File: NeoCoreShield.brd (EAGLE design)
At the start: 70.9 x 72.1 mm, 45 parts, among them J1 PXC-PTSM-04-RA-1778641, J10 MAGJACK, J2 PXC-PTSM-04-RA-1778641, J3 PXC-PTSM-04-RA-1778641, J4 PXC-PTSM-04-RA-1778641, J5 PXC-PTSM-04-RA-1778641, Q1 2.5A/30V/105mΩ, Q2 310mA/60V/1.6Ω, Q3 2.5A/30V/105mΩ, Q4 2.5A/30V/105mΩ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

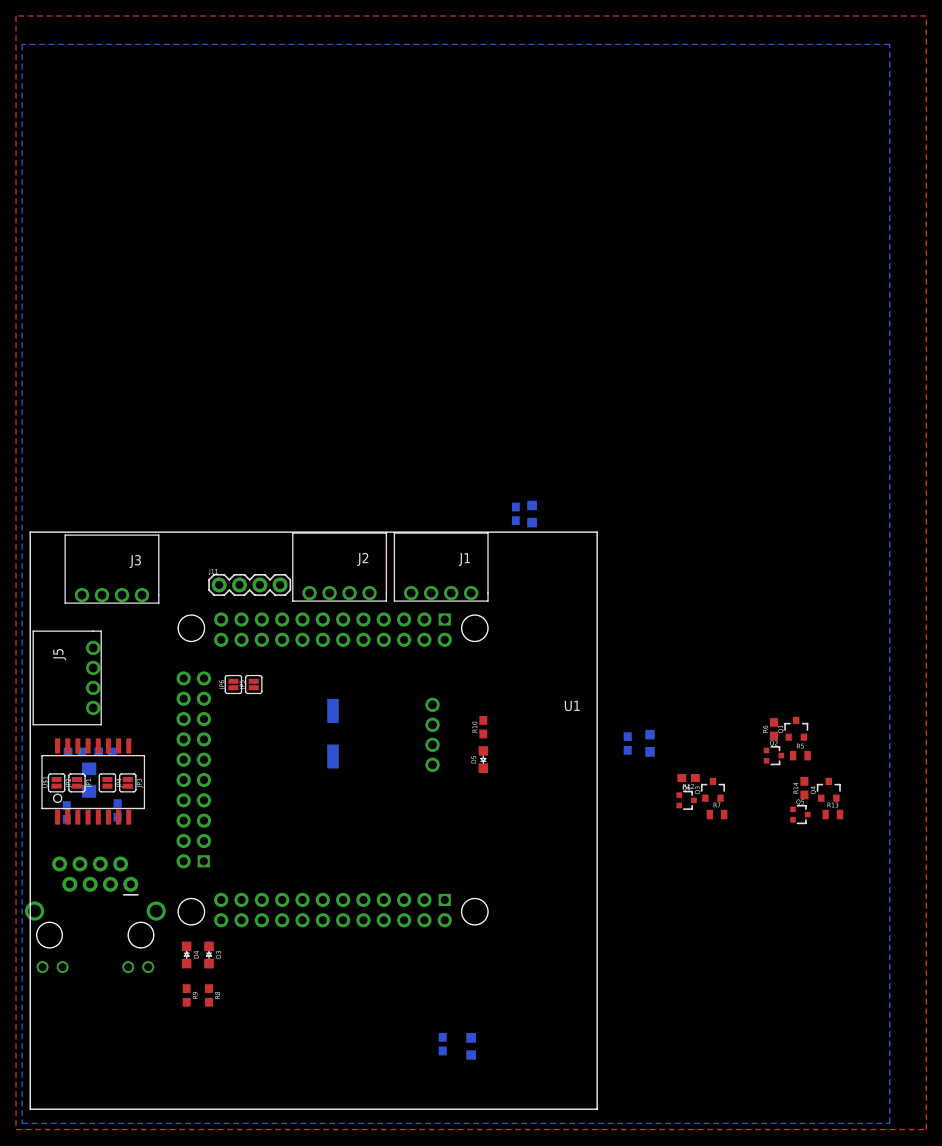
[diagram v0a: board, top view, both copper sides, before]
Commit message: Routed Neo Core Shields
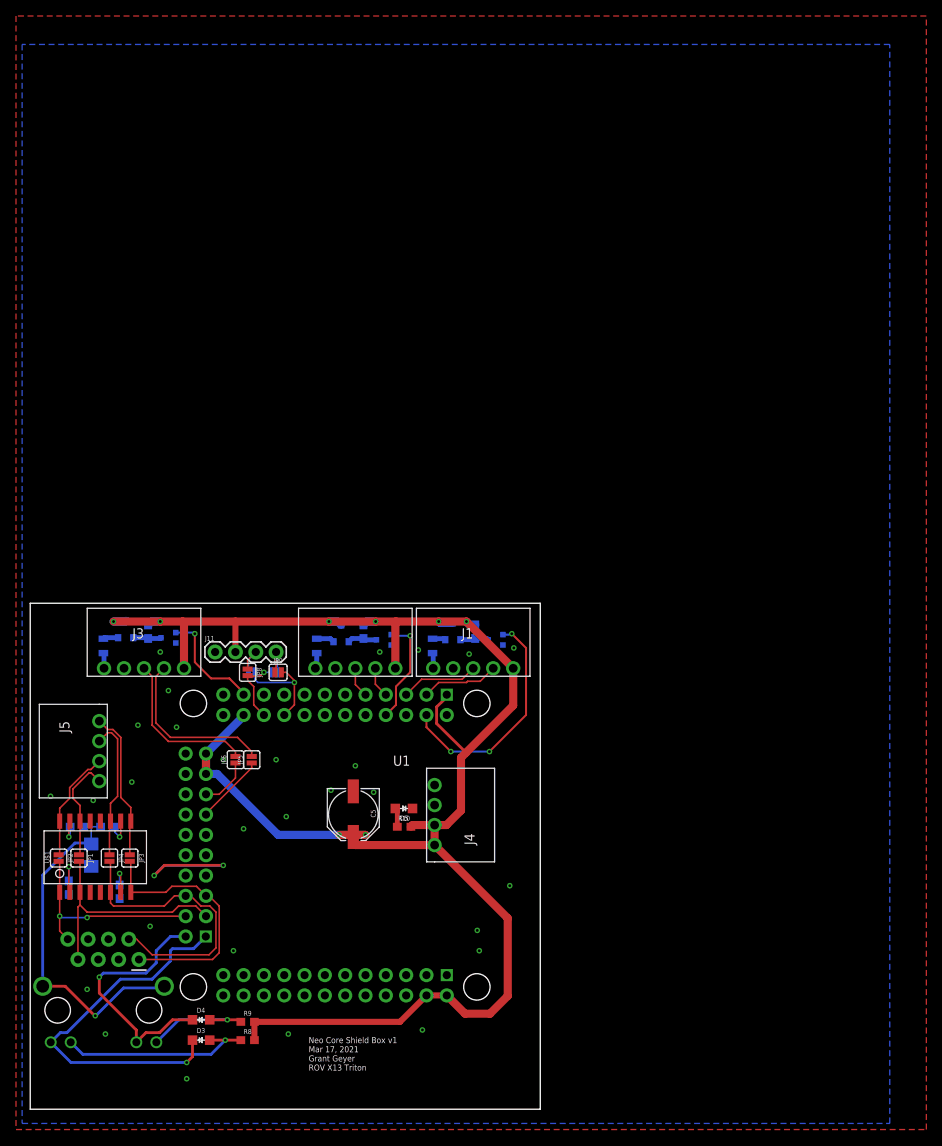
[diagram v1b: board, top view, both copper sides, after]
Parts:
- removed D1, D2, D6: BLUE, LED-0805:0805
- removed R11, R3, R4: 470, SparkFun-Resistors:0603
- added JP10, JP7, JP8, JP9: JUMPER-SMT_2_NO_SILK, SparkFun-Jumpers:SMT-JUMPER_2_NO_SILK
- J1, J2, J3: value PXC-PTSM-04-RA-1778641 -> PXC-PTSM-05-RA; device Phoenix Contact PTSM-04-V-1778573:PXC-PTSM-04-RA-1778641 -> Phoenix Contact PTSM 5 pin:PXC-PTSM-05-RA
- moved R7 79.6 mm to (9.14, 57.9), flipped to the bottom, turned to 270 degrees
- moved Q3 76.1 mm to (11.9, 59.9), flipped to the bottom
- moved R12 70.0 mm to (14.7, 59.7), flipped to the bottom, turned to 90 degrees
- moved Q6 67.9 mm to (17.3, 58.9), flipped to the bottom
- moved R5 62.0 mm to (35.8, 57.9), flipped to the bottom, turned to 270 degrees
- moved Q1 58.1 mm to (38.9, 59.4), flipped to the bottom
- moved R13 54.3 mm to (50.3, 57.9), flipped to the bottom, turned to 270 degrees
- moved R6 52.7 mm to (41.7, 59.7), flipped to the bottom
- moved Q4 51.0 mm to (52.8, 59.7), flipped to the bottom
- moved Q2 50.9 mm to (44.2, 58.7), flipped to the bottom
- moved R14 45.6 mm to (55.6, 59.7), flipped to the bottom
- moved Q5 43.9 mm to (58.2, 58.7), flipped to the bottom
- moved J4 17.5 mm to (50.5, 33.0), flipped to the top, turned to 90 degrees
- moved R10 15.9 mm to (46.7, 35.3), turned to 0 degrees
- moved D5 11.6 mm to (46.7, 37.6), turned to 180 degrees
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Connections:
- removed net CONN_SENSE1: R11.2
- removed net CONN_SENSE2: R3.2
- removed net CONN_SENSE3: R4.2
- removed net N$1: D1.A, R3.1
- removed net N$2: D2.A, R4.1
- removed net N$4: D6.A, R11.1
- new net UART_RX_TX: J11.3, JP7.1, JP8.1
- new net UART_TX_RX: J11.4, JP10.1, JP9.1
- net GND: no longer D1.C, D2.C, D6.C
- net LED_1: now also J1.5
- net LED_2: now also J2.5
- net LED_3: now also J3.5
- net LED_CONTROL1: now also U1.4
- net LED_CONTROL2: now also U1.8
- net LED_CONTROL3: now also U1.21
- net UART_RX: now also JP7.2, JP9.2; no longer J11.4
- net UART_TX: now also JP10.2, JP8.2; no longer J11.3
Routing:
- net 5V: track 0.00 -> 226.5 mm, vias 0 -> 8
- net LINK: track 0.00 -> 46.7 mm, vias 0 -> 1
- net ETH_TERM_MID: track 0.00 -> 44.1 mm, vias 0 -> 1
- net RD_N: track 0.00 -> 36.5 mm
- net RD_P: track 0.00 -> 32.5 mm
- net SPEED: track 0.00 -> 32.0 mm, vias 0 -> 1
- net TD_P: track 0.00 -> 29.4 mm
- net LED_CONTROL1: track 0.00 -> 29.2 mm, vias 0 -> 3
- net TD_N: track 0.00 -> 26.1 mm, vias 0 -> 2
- net LINK_MID: track 0.00 -> 24.6 mm, vias 0 -> 1
- net USB_CAM_3_P: track 0.00 -> 21.3 mm
- net USB_CAM_3_N: track 0.00 -> 19.9 mm
- net RX_P: track 0.00 -> 18.8 mm
- net GND: track 0.00 -> 18.3 mm, vias 0 -> 30
- net RX_N: track 0.00 -> 18.0 mm
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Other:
- board size 70.9 x 72.1 mm -> 63.8 x 63.2 mm
- board text added: "Neo Core Shield Box v1 Mar 17, 2021 Grant Geyer ROV X13 Triton"

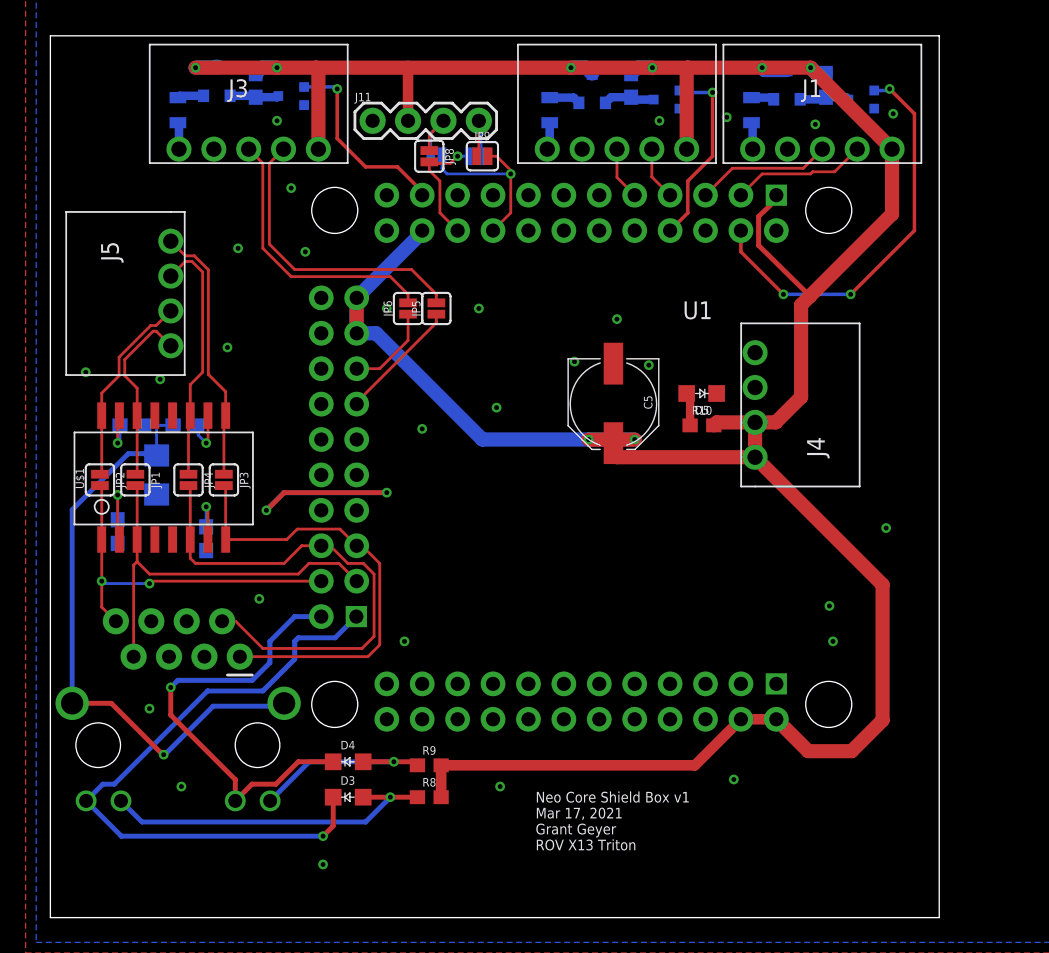
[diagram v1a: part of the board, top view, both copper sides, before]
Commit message: Neo Core Nano Pi Shield order
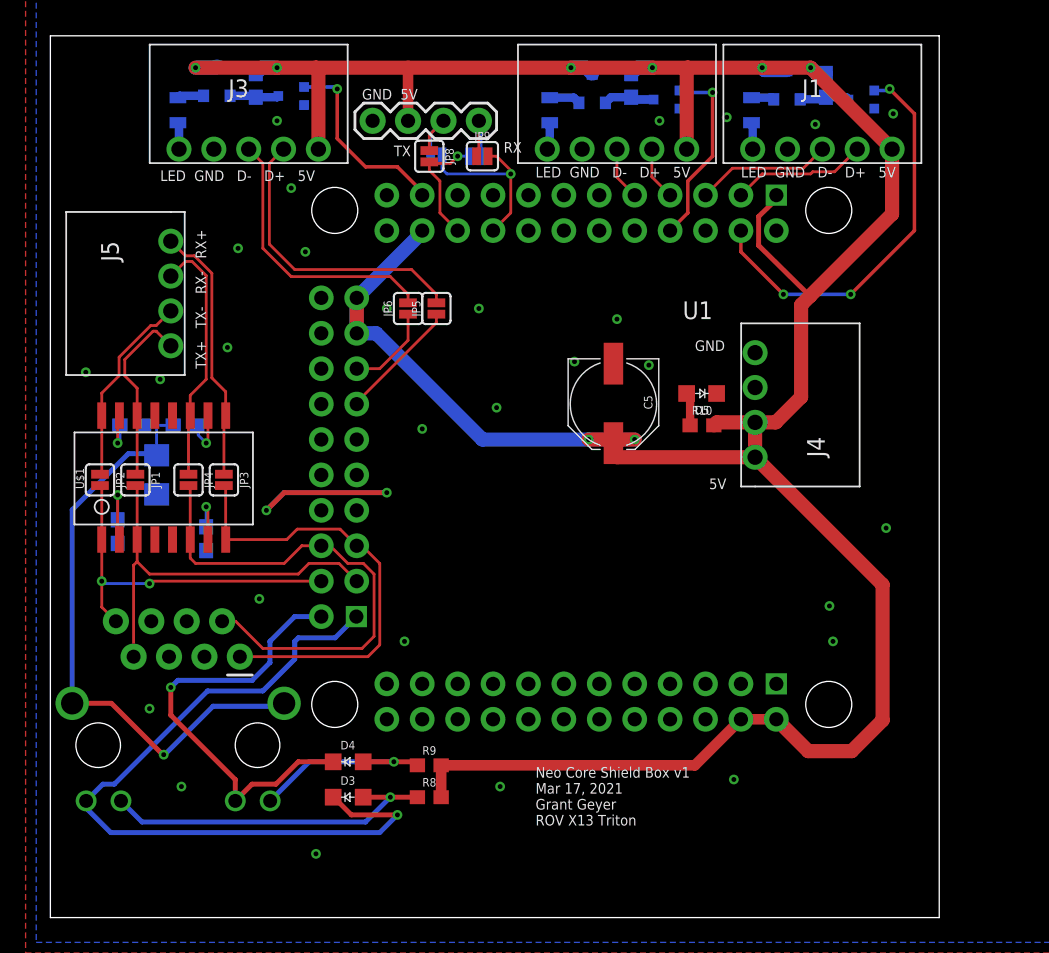
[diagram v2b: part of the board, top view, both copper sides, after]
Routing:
- net LINK: track 46.7 -> 54.8 mm
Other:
- board text added: "5V"
- board text added: "GND"
- board text added: "GND 5V"
- board text added: "LED GND D- D+ 5V"
- board text added: "RX"
- board text added: "TX"
- board text added: "TX+ TX- RX- RX+"
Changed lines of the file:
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@@
 <wire x1="63.754" y1="63.246" x2="0" y2="63.246" width="0" layer="20"/>
 <wire x1="0" y1="63.246" x2="0" y2="0" width="0" layer="20"/>
-<text x="34.798" y="4.826" size="0.762" layer="25">Neo Core Shield Box v1
+<text x="34.798" y="6.604" size="0.762" layer="25">Neo Core Shield Box v1
 Mar 17, 2021
 Grant Geyer
 ROV X13 Triton</text>
+<text x="11.176" y="39.37" size="0.762" layer="25" rot="R90">TX+   TX-   RX-   RX+</text>
+<text x="7.874" y="52.832" size="0.762" layer="25">LED  GND   D-   D+   5V</text>
+<text x="34.798" y="53.086" size="0.762" layer="25">LED  GND   D-   D+   5V</text>
+<text x="49.53" y="53.086" size="0.762" layer="25">LED  GND   D-   D+   5V</text>
+<text x="46.228" y="40.64" size="0.762" layer="25">GND</text>
+<text x="47.244" y="30.734" size="0.762" layer="25">5V</text>
+<text x="24.638" y="54.61" size="0.762" layer="25">TX</text>
+<text x="32.512" y="54.864" size="0.762" layer="25">RX</text>
+<text x="22.352" y="58.674" size="0.762" layer="25">GND  5V</text>
 </plain>
 <attributes>
@@
 </element>
 <element name="J11" library="SparkFun-Connectors" library_urn="urn:adsk.eagle:library:513" package="1X04" package3d_urn="urn:adsk.eagle:package:38085/1" value="" x="23.114" y="57.15" smashed="yes">
-<attribute name="NAME" x="21.844" y="58.547" size="0.6096" layer="25" font="vector" ratio="20"/>
 <attribute name="PROD_ID" value="CONN-09696" x="23.114" y="73.406" size="1.778" layer="27" display="off"/>
 <attribute name="VALUE" x="21.844" y="55.118" size="0.6096" layer="27" font="vector" ratio="20"/>
@@
 <via x="7.112" y="14.986" extent="1-16" drill="0.35"/>
 <via x="9.398" y="9.398" extent="1-16" drill="0.35"/>
-<via x="19.558" y="3.81" extent="1-16" drill="0.35"/>
+<via x="19.05" y="4.572" extent="1-16" drill="0.35"/>
 <via x="32.258" y="9.398" extent="1-16" drill="0.35"/>
 <via x="49.022" y="9.906" extent="1-16" drill="0.35"/>
@@
 <contactref element="J5" pad="1"/>
 <wire x1="8.636" y1="48.514" x2="9.6828" y2="47.4672" width="0.2032" layer="1"/>
-<wire x1="10.3283375" y1="47.4672" x2="11.3284" y2="46.4671375" width="0.2032" layer="1"/>
+<wire x1="10.3283375" y1="47.4672" x2="11.5824" y2="46.2131375" width="0.2032" layer="1"/>
 <wire x1="9.6828" y1="47.4672" x2="10.3283375" y2="47.4672" width="0.2032" layer="1"/>
 <wire x1="12.573" y1="37.719" x2="12.573" y2="36.006" width="0.2032" layer="1"/>
-<wire x1="11.3284" y1="46.4671375" x2="11.3284" y2="38.9636" width="0.2032" layer="1"/>
-<wire x1="11.3284" y1="38.9636" x2="12.573" y2="37.719" width="0.2032" layer="1"/>
+<wire x1="11.5824" y1="46.2131375" x2="11.5824" y2="38.7096" width="0.2032" layer="1"/>
+<wire x1="11.5824" y1="38.7096" x2="12.573" y2="37.719" width="0.2032" layer="1"/>
 <wire x1="12.446" y1="31.8008" x2="12.446" y2="35.879" width="0.2032" layer="1"/>
 <wire x1="12.446" y1="35.879" x2="12.573" y2="36.006" width="0.2032" layer="1"/>
@@
 <wire x1="8.636" y1="46.014" x2="9.6828" y2="47.0608" width="0.2032" layer="1"/>
 <wire x1="9.6828" y1="47.0608" x2="10.16" y2="47.0608" width="0.2032" layer="1"/>
-<wire x1="10.16" y1="47.0608" x2="10.922" y2="46.2988" width="0.2032" layer="1"/>
-<wire x1="10.922" y1="39.116" x2="10.922" y2="46.2988" width="0.2032" layer="1"/>
-<wire x1="10.033" y1="36.006" x2="10.033" y2="38.227" width="0.2032" layer="1"/>
-<wire x1="10.033" y1="38.227" x2="10.922" y2="39.116" width="0.2032" layer="1"/>
+<wire x1="10.16" y1="47.0608" x2="11.176" y2="46.0448" width="0.2032" layer="1"/>
+<wire x1="11.176" y1="46.0448" x2="11.176" y2="38.608" width="0.2032" layer="1"/>
+<wire x1="10.033" y1="36.006" x2="10.033" y2="37.465" width="0.2032" layer="1"/>
+<wire x1="10.033" y1="37.465" x2="11.176" y2="38.608" width="0.2032" layer="1"/>
 <wire x1="9.906" y1="31.8008" x2="9.906" y2="35.879" width="0.2032" layer="1"/>
 <wire x1="9.906" y1="35.879" x2="10.033" y2="36.006" width="0.2032" layer="1"/>
@@
 <wire x1="15.24" y1="16.256" x2="17.526" y2="18.542" width="0.3556" layer="16"/>
 <wire x1="17.78" y1="20.066" x2="20.4216" y2="20.066" width="0.3556" layer="16"/>
-<wire x1="2.564" y1="8.37" x2="5.092" y2="5.842" width="0.3556" layer="16"/>
-<wire x1="19.558" y1="5.842" x2="5.092" y2="5.842" width="0.3556" layer="16"/>
-<via x="19.558" y="5.842" extent="1-16" drill="0.35"/>
-<wire x1="20.286" y1="8.636" x2="20.286" y2="6.57" width="0.3556" layer="1"/>
-<wire x1="20.286" y1="6.57" x2="19.558" y2="5.842" width="0.3556" layer="1"/>
+<wire x1="4.33" y1="6.096" x2="2.564" y2="7.862" width="0.3556" layer="16"/>
+<wire x1="2.564" y1="8.37" x2="2.564" y2="7.862" width="0.3556" layer="16"/>
+<wire x1="24.892" y1="7.366" x2="23.622" y2="6.096" width="0.3556" layer="16"/>
+<wire x1="23.622" y1="6.096" x2="4.33" y2="6.096" width="0.3556" layer="16"/>
+<via x="24.892" y="7.366" extent="1-16" drill="0.35"/>
+<wire x1="24.892" y1="7.366" x2="21.59" y2="7.366" width="0.3556" layer="1"/>
+<wire x1="21.59" y1="7.366" x2="20.32" y2="8.636" width="0.3556" layer="1"/>
+<wire x1="20.286" y1="8.636" x2="20.32" y2="8.636" width="0.3556" layer="1"/>
 </signal>
 <signal name="SPEED">
